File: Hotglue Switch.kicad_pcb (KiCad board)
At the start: 2 copper layers, 26 x 10.2 mm, 10 parts, among them J3 BATTERY, J8 +OUTPUT, J9 -OUTPUT, M1 Screw, M2 Screw

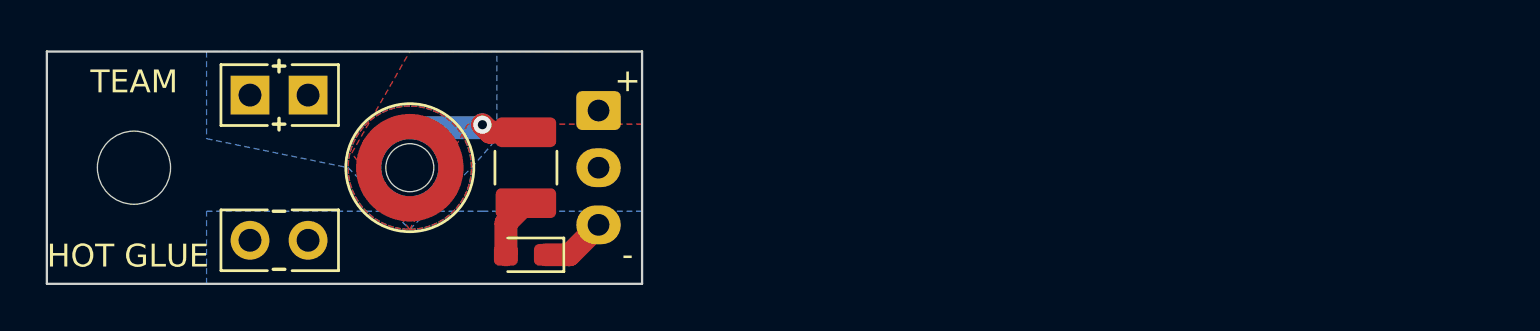
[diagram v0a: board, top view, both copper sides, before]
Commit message: update project and pcb files for rev 1.1
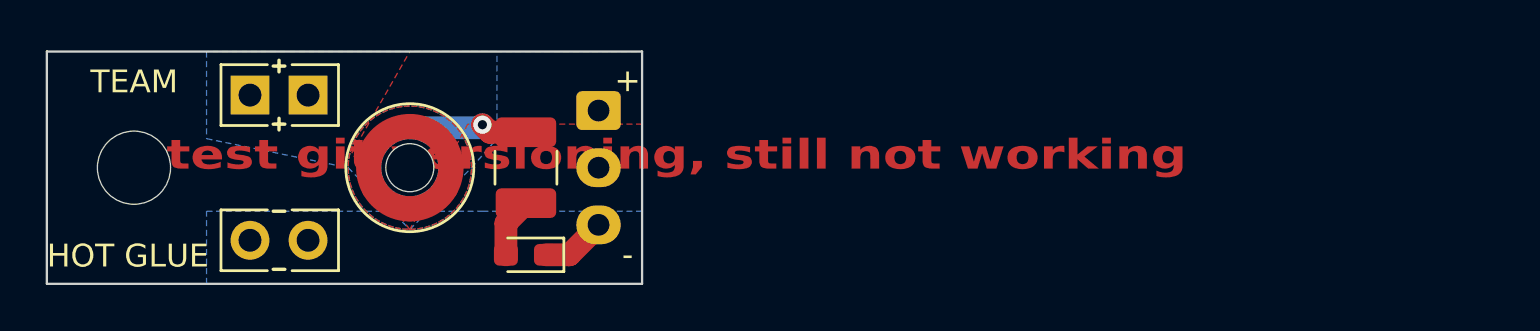
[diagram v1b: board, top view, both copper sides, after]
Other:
- board text added: "test git versioning, still not working"

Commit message: commit of all modified files for rev 1.1, including gerbers, 3d step models, PCB, schematic, and project files.
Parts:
- D1: value 150060GS75003 -> XL-1608UBC-06A
- H1: value MountingHole -> M2 MountingHole; footprint MountingHole:MountingHole_3.2mm_M3_DIN965 -> MountingHole:MountingHole_2.2mm_M2_DIN965
- H2: footprint Trent_Components_Library:screw_contact_3 -> Trent-footprints:Sinhoo-M1.6-screw-contact
- H4: value 9774010633R -> SMTSO1610MTJ; footprint Mounting_Wuerth:Mounting_Wuerth_WA-SMSI-M1.6_H1mm_9774010633 -> Trent-footprints:Mounting_Sinhoo_SMTSO1610MJT
- J3: footprint Trent_Components_Library:JST_XH_S3B-XH-A-1_1x03_P2.50mm_Horizontal_Aliexpress -> Trent-footprints:JST_XH_S3B-XH-A-1_1x03_P2.50mm_Horizontal_Aliexpress
- J8: footprint Trent_Components_Library:PinHeader_1x02_P2.54mm_Vertical Positive -> Trent-footprints:PinHeader_1x02_P2.54mm_Vertical Positive
- J9: footprint Trent_Components_Library:PinHeader_1x02_P2.54mm_Vertical Negative -> Trent-footprints:PinHeader_1x02_P2.54mm_Vertical Negative
- M1: value Screw -> M1.6 Screw; footprint Trent_Components_Library:Screw M1.6 -> Trent-footprints:Screw M1.6
- M2: value Screw -> M2 Screw; footprint Trent_Components_Library:Screw M3 -> Trent-footprints:Screw M2
- R1: value 560112140008 -> RC0603FR-07390RL; footprint Resistor_SMD:R_1210_3225Metric_Pad1.30x2.65mm_HandSolder -> Resistor_SMD:R_0603_1608Metric_Pad0.98x0.95mm_HandSolder
- moved H1 3.67 mm to (72.2, 50.8)
- moved M2 3.67 mm to (72.2, 50.8)
- moved J8 2.32 mm to (76.0, 47.6)
- moved J9 2.32 mm to (76.0, 54.0)
- moved H2 2.11 mm to (82.8, 50.8)
- moved H4 2.11 mm to (82.8, 50.8)
- moved M1 2.11 mm to (82.8, 50.8)
- moved D1 1.48 mm to (86.8, 53.6), turned to 90 degrees
- moved R1 1.34 mm to (86.8, 50.0)
- moved J3 0.10 mm to (89.0, 48.3)
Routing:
- net /BATT SWITCH: track 5.27 -> 3.13 mm
- net Net-(D1-A): track 2.62 -> 1.81 mm
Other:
- board size 26 x 10.2 mm -> 21 x 10.2 mm
- board text added: "ANT SWITCH"
- board text added: "v1.1"
- board text removed: "ANTSWITCH"
- board text removed: "test git versioning, still not working"
- board text removed: "v1.0"
